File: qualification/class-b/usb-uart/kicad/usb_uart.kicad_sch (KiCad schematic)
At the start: 32 parts, among them J1 TYPE-C-31-M-12, J2 UART1, J3 FLOW1, J4 RS485, U1 CH342F, U2 LDO, U3 THVD1450D

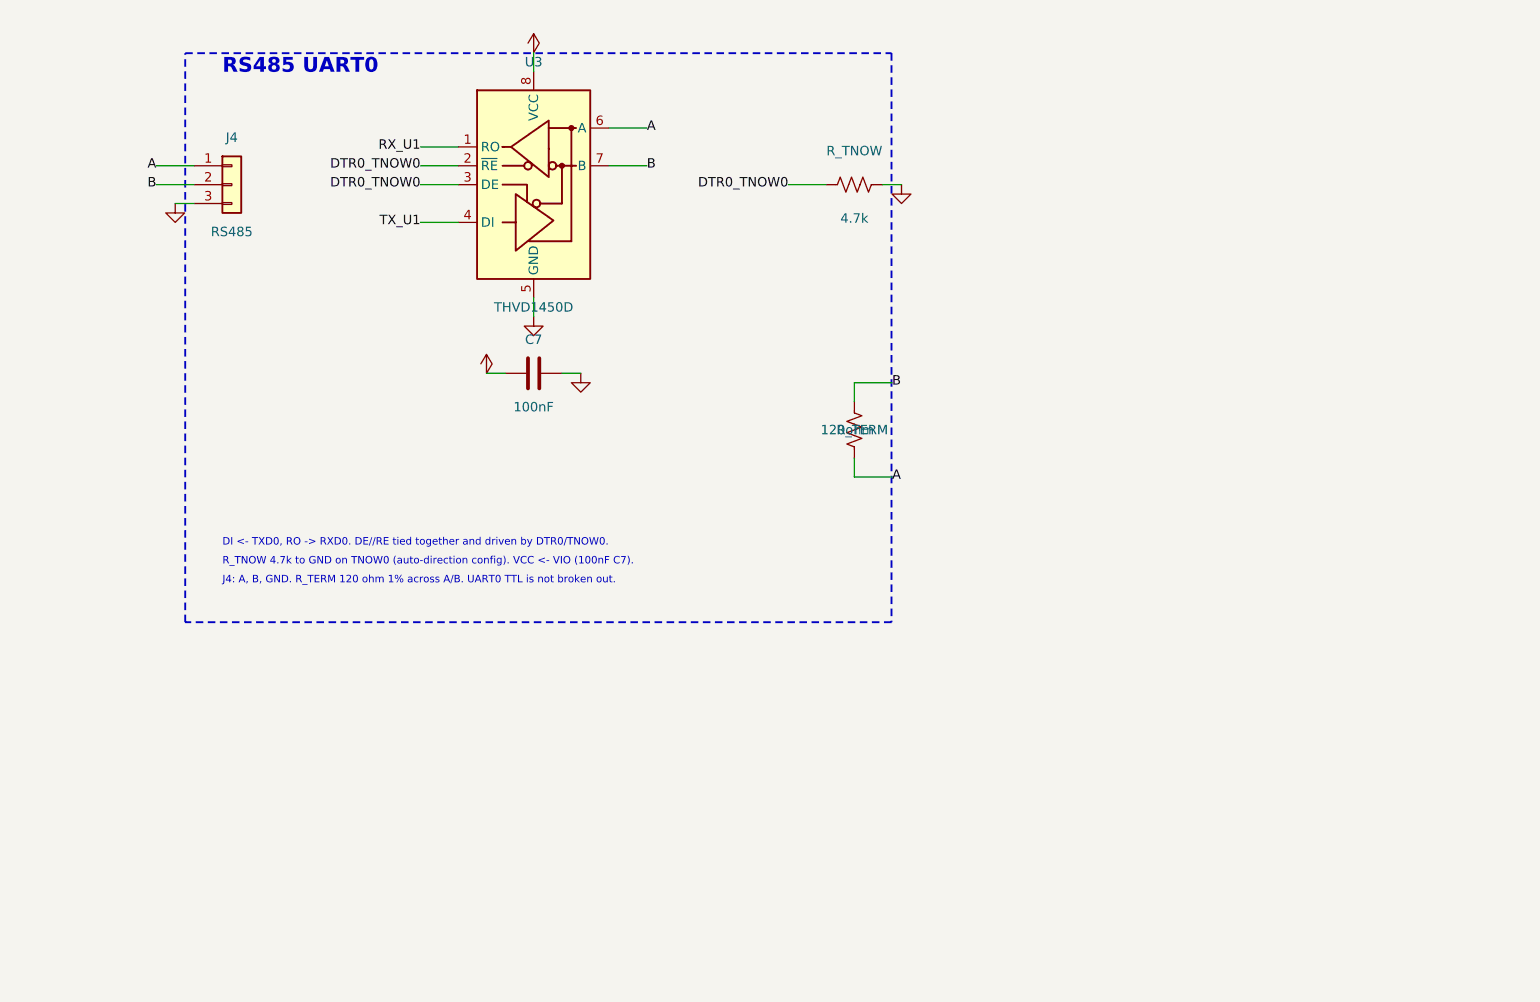
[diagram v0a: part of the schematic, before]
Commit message: SYN-66 - Switchable RS-485 termination, A/B surge protection, qualification matrix and hashes
Address the review of #103.

Board: R_TERM now sits behind a 2-pin jumper (J_TERM), so the board can be used away from the ends of a bus. A and B get 10 ohm series resistors and a Bourns CDSOT23-SM712 TVS array on the bus side, following TI's 1 kV surge circuit for the THVD1450 (SLLSEY3E fig. 37). The series resistors matter: the THVD1450 bus pins are rated +/-18 V and the SM712 clamps at 19 V to 26 V. Not surge-tested; the resistors are generic 0603.

Registry: add header_1x2 and cdsot23_sm712, and tag the THVD1450 A/B pins rs485_a and rs485_b for the RS-485 checks in #140.

Evidence: QUALIFICATION.md separates what Synth and KiCad checked from what needs SI/PI/RF or manufacturer review, SHA256SUMS records the artifact hashes, and reports/ holds the release gate and DRC records.

The revised board routes with 0 open nets but does not pass the release gate: KiCad reports 2 unconnected ground-pour items in every completed route. This is disclosed in the README and the matrix, not fixed. Needs absmach/synth#139 and #140 for the fabrication note and the RS-485 checks.

Signed-off-by: nyagamunene <stevenyaga2014@gmail.com>
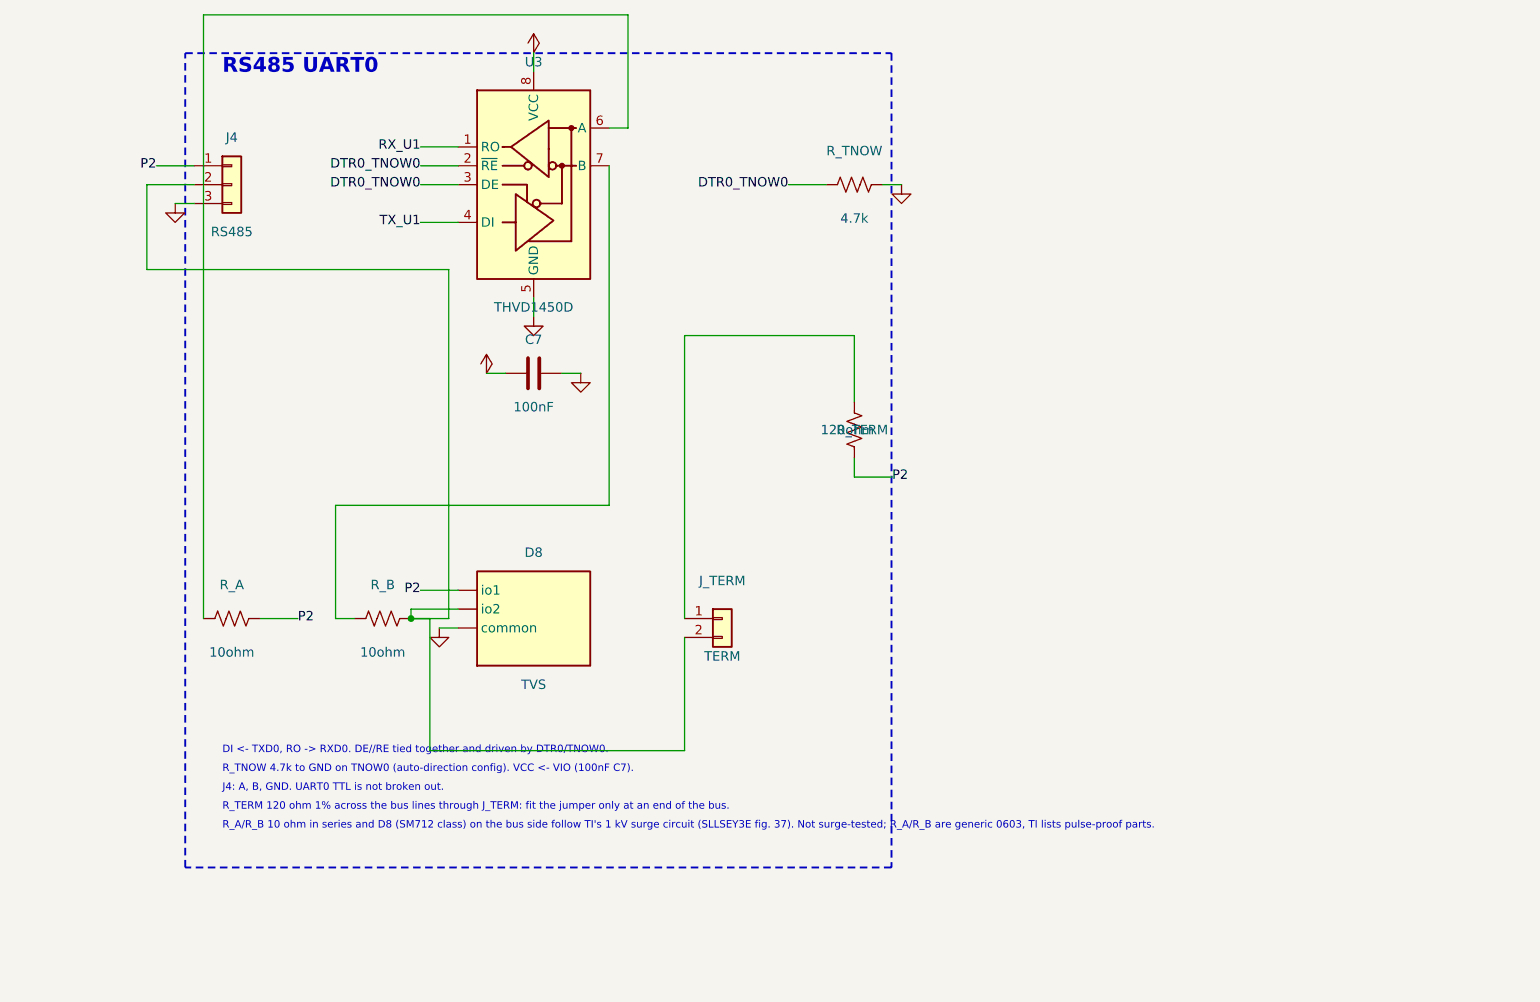
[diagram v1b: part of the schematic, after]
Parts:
- added D8: TVS, Package_TO_SOT_SMD:SOT-23, symbol synth:cdsot23_sm712
- added J_TERM: TERM, Connector_PinHeader_2.54mm:PinHeader_1x02_P2.54mm_Vertical, symbol Connector_Generic:Conn_01x02
- added R_A, R_B: 10ohm, Resistor_SMD:R_0603_1608Metric, symbol Device:R_US
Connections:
- net GND: now also D8.3 (common)
- net A renamed P2
- net P2: now also D8.1 (io1), R_A.2; no longer U3.6 (A)
- removed net B: J4.2 (Pin_2), R_TERM.2, U3.7 (B)
- new net: D8.2 (io2), J4.2 (Pin_2), J_TERM.2 (Pin_2), R_B.2
- new net: J_TERM.1 (Pin_1), R_TERM.2
- new net: R_B.1, U3.7 (B)
- new net: R_A.1, U3.6 (A)
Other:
- note added: "J4: A, B, GND. UART0 TTL is not broken out."
- note added: "R_A/R_B 10 ohm in series and D8 (SM712 class) on the bus side follow TI's 1 kV surge circuit (SLLSEY3E fig. 37). Not surge-tested; R_A/R_B are generic 0603, TI lists pulse-proof parts."
- note added: "R_TERM 120 ohm 1% across the bus lines through J_TERM: fit the jumper only at an end of the bus."
- note removed: "J4: A, B, GND. R_TERM 120 ohm 1% across A/B. UART0 TTL is not broken out."

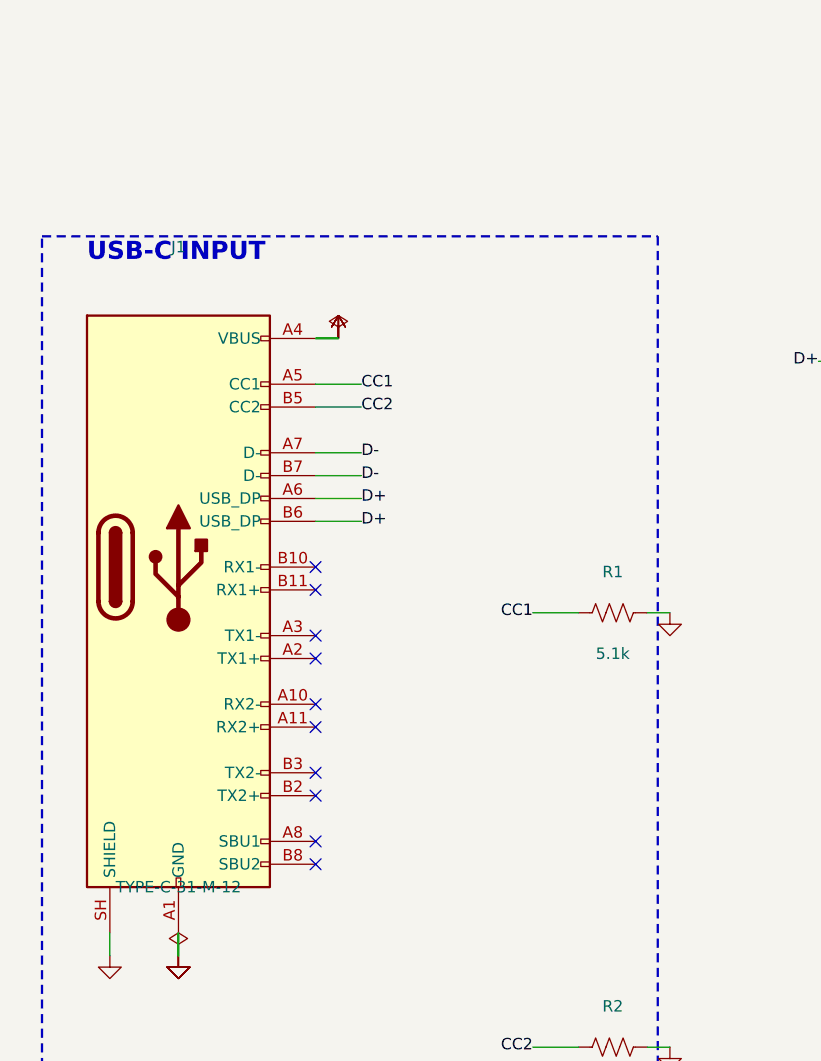
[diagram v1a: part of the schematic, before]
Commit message: SYN-66 - Use the Amphenol USB-C connector with its 3D model, centre it, add mounting holes, re-route
The HRO TYPE-C-31-M-12 has no 3D model anywhere in KiCad's library, and the GCT USB4105 puts its NPTH holes 0.175 mm from its pads, under JLCPCB's 0.2 mm. The board now uses the Amphenol 12401610E4#2A (new registry part, datasheet not read: the manufacturer's site refuses requests). J1 is centred on the top edge, four M2.5 mounting holes are added, VBUS is routed at 0.3 mm to fit the connector's 0.3 mm contacts, and the board is re-routed: 29 nets, 0 open, DRC 0 errors and 0 unconnected, release gate passed. README, qualification matrix, reports, render and hashes are updated; they depend on PR #154 and PR #162, which are not merged yet.

Signed-off-by: nyagamunene <stevenyaga2014@gmail.com>
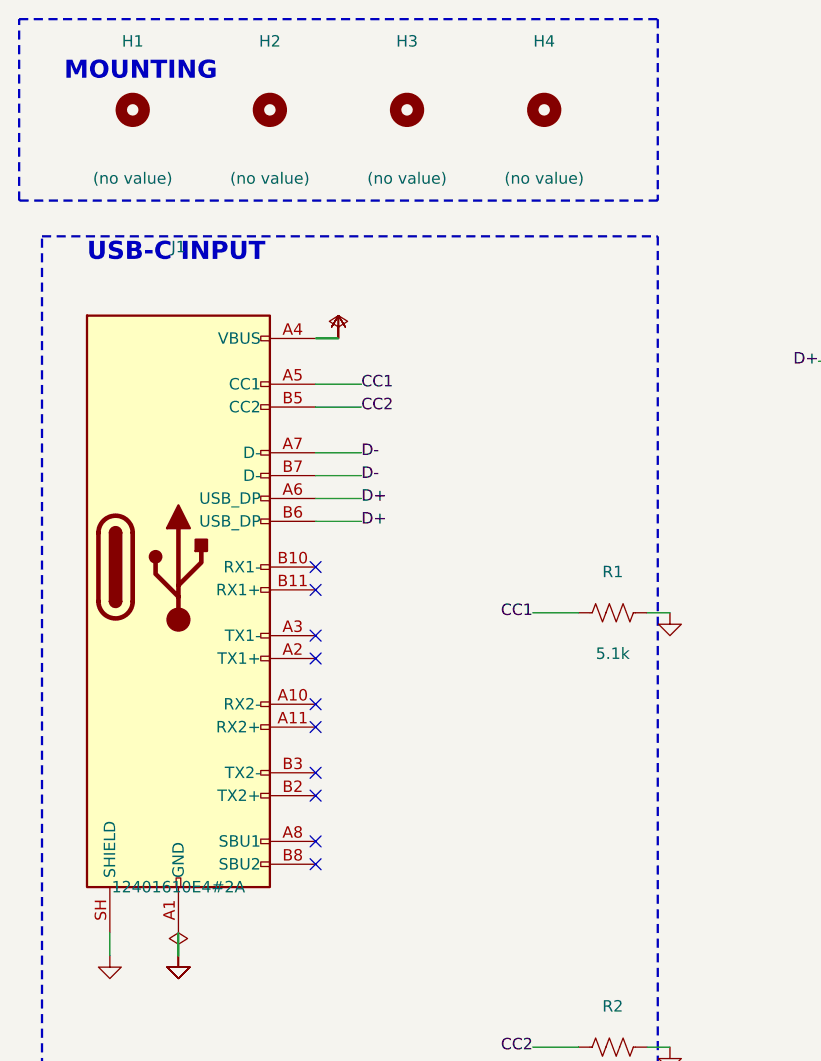
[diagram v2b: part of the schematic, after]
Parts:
- added H1, H2, H3, H4: (no value), MountingHole:MountingHole_2.5mm, symbol Mechanical:MountingHole
- J1: value TYPE-C-31-M-12 -> 12401610E4#2A; footprint Connector_USB:USB_C_Receptacle_HRO_TYPE-C-31-M-12 -> Connector_USB:USB_C_Receptacle_Amphenol_12401610E4-2A; LCSC C165948 -> (none); MPN TYPE-C-31-M-12 -> 12401610E4#2A
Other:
- note added: "MOUNTING"

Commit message: SYN-66 - Use M3 mounting holes, re-route, and replace every picture
The four mounting holes are now M3 (3.2 mm), a new registry part. The board is re-placed and re-routed (the first M3 layout that passed was the 23rd tried): 29 nets, 0 open, DRC 0 errors and 0 unconnected, release gate passed. All pictures are new: 3D top, angled and bottom views, top and bottom copper, and the schematic; the STEP, reports, hashes, README and qualification matrix match the board. The USB pair is badly skewed (13.5 mm) and the docs say so.

Signed-off-by: nyagamunene <stevenyaga2014@gmail.com>
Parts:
- H1, H2, H3, H4: footprint MountingHole:MountingHole_2.5mm -> MountingHole:MountingHole_3.2mm_M3
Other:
- moved on the sheet: H1, H2, H3, H4
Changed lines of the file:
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@@
 	(symbol
 		(lib_id "Mechanical:MountingHole")
-		(at 30.48 5.08 0)
+		(at 30.48 214.63 0)
 		(unit 1)
 		(in_bom yes)
@@
 			"Reference"
 			"H1"
-			(at 30.48 -2.54 0)
+			(at 30.48 207.01 0)
 			(effects
 				(font
@@
 			"Value"
 			"(no value)"
-			(at 30.48 12.7 0)
+			(at 30.48 222.25 0)
 			(effects
 				(font
@@
 		(property
 			"Footprint"
-			"MountingHole:MountingHole_2.5mm"
-			(at 30.48 5.08 0)
+			"MountingHole:MountingHole_3.2mm_M3"
+			(at 30.48 214.63 0)
 			(effects
 				(font
@@
 			"Datasheet"
 			""
-			(at 30.48 5.08 0)
+			(at 30.48 214.63 0)
 			(effects
 				(font
@@
 			"MPN"
 			""
-			(at 30.48 5.08 0)
+			(at 30.48 214.63 0)
 			(effects
 				(font
@@
 			"LCSC"
 			""
-			(at 30.48 5.08 0)
+			(at 30.48 214.63 0)
 			(effects
 				(font
@@
 	(symbol
 		(lib_id "Mechanical:MountingHole")
-		(at 45.72 5.08 0)
+		(at 45.72 214.63 0)
 		(unit 1)
 		(in_bom yes)
@@
 			"Reference"
 			"H2"
-			(at 45.72 -2.54 0)
+			(at 45.72 207.01 0)
 			(effects
 				(font
@@
 			"Value"
 			"(no value)"
-			(at 45.72 12.7 0)
+			(at 45.72 222.25 0)
 			(effects
 				(font
@@
 		(property
 			"Footprint"
-			"MountingHole:MountingHole_2.5mm"
-			(at 45.72 5.08 0)
+			"MountingHole:MountingHole_3.2mm_M3"
+			(at 45.72 214.63 0)
 			(effects
 				(font
@@
 			"Datasheet"
 			""
-			(at 45.72 5.08 0)
+			(at 45.72 214.63 0)
 			(effects
 				(font
@@
 			"MPN"
 			""
-			(at 45.72 5.08 0)
+			(at 45.72 214.63 0)
 			(effects
 				(font
@@
 			"LCSC"
 			""
-			(at 45.72 5.08 0)
+			(at 45.72 214.63 0)
 			(effects
 				(font
@@
 	(symbol
 		(lib_id "Mechanical:MountingHole")
-		(at 60.96 5.08 0)
+		(at 60.96 214.63 0)
 		(unit 1)
 		(in_bom yes)
@@
 			"Reference"
 			"H3"
-			(at 60.96 -2.54 0)
+			(at 60.96 207.01 0)
 			(effects
 				(font
@@
 			"Value"
 			"(no value)"
-			(at 60.96 12.7 0)
+			(at 60.96 222.25 0)
 			(effects
 				(font
@@
 		(property
 			"Footprint"
-			"MountingHole:MountingHole_2.5mm"
-			(at 60.96 5.08 0)
+			"MountingHole:MountingHole_3.2mm_M3"
+			(at 60.96 214.63 0)
 			(effects
 				(font
@@
 			"Datasheet"
 			""
-			(at 60.96 5.08 0)
+			(at 60.96 214.63 0)
 			(effects
 				(font
@@
 			"MPN"
 			""
-			(at 60.96 5.08 0)
+			(at 60.96 214.63 0)
 			(effects
 				(font
@@
 			"LCSC"
 			""
-			(at 60.96 5.08 0)
+			(at 60.96 214.63 0)
 			(effects
 				(font
@@
 	(symbol
 		(lib_id "Mechanical:MountingHole")
-		(at 76.2 5.08 0)
+		(at 76.2 214.63 0)
 		(unit 1)
 		(in_bom yes)
@@
 			"Reference"
 			"H4"
-			(at 76.2 -2.54 0)
+			(at 76.2 207.01 0)
 			(effects
 				(font
@@
 			"Value"
 			"(no value)"
-			(at 76.2 12.7 0)
+			(at 76.2 222.25 0)
 			(effects
 				(font
@@
 		(property
 			"Footprint"
-			"MountingHole:MountingHole_2.5mm"
-			(at 76.2 5.08 0)
+			"MountingHole:MountingHole_3.2mm_M3"
+			(at 76.2 214.63 0)
 			(effects
 				(font
@@
 			"Datasheet"
 			""
-			(at 76.2 5.08 0)
+			(at 76.2 214.63 0)
 			(effects
 				(font
@@
 			"MPN"
 			""
-			(at 76.2 5.08 0)
+			(at 76.2 214.63 0)
 			(effects
 				(font
@@
 			"LCSC"
 			""
-			(at 76.2 5.08 0)
+			(at 76.2 214.63 0)
 			(effects
 				(font
@@
 	(text
 		"MOUNTING"
-		(at 22.86 2 0)
+		(at 22.86 207.92 0)
 		(effects
 			(font
@@
 	)
 	(rectangle
-		(start 17.86 -5)
-		(end 88.82 15.16)
+		(start 17.86 204.92)
+		(end 88.82 225.08)
 		(stroke
 			(width 0.254)

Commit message: SYN-66 - Route the board again with ground vias, screw-head keepouts and TX LEDs on data
Route the board with the four integrated tool PRs (#154, #162, #175, #176). Every outer SMD ground pad now has a ground via within 2 mm, the corner vias are clear of the M3 holes, and the result is 0 open nets, KiCad DRC 0 errors, release gate passed.

The TX LEDs now run from VIO into TXD0 and TXD1, so they light only while data goes out. USB path lengths per connector contact, the ground tie table, the 134 ERC warnings and the unconfirmed J1 oval hole and via annular ring questions are in the README and QUALIFICATION.md. New pictures, STEP and SHA256SUMS match the delivered board.

Signed-off-by: nyagamunene <stevenyaga2014@gmail.com>
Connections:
- net GND: no longer D4.1 (K), D7.1 (K)
- net TX: now also D7.1 (K); no longer R7.1
- net TX_U1: now also D4.1 (K); no longer R4.1
- net VIO: now also R4.1, R7.1
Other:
- note added: "D4/D7 red LEDs from VIO into TXD0/TXD1: TXD idles high, so they light only while data goes out."
- note removed: "D4/D7 red LEDs from TXD0/TXD1."
